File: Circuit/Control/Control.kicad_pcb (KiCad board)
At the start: 2 copper layers, 25.4 x 22.9 mm, 12 parts, among them J1 Signal, J2 12V NO G, SW1 Force on, U1 NE555

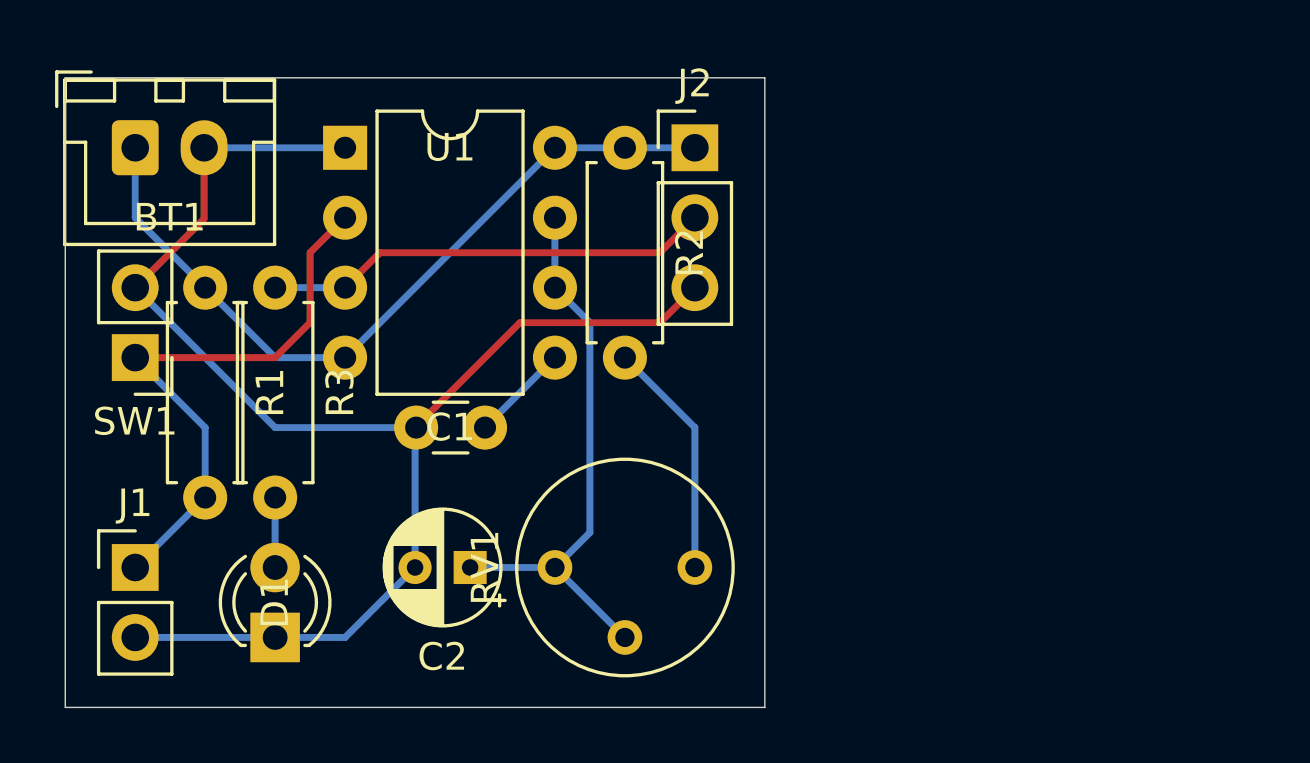
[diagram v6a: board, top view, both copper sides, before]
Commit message: [Circuit] Change the interface between control module, switch module, and discharge signal
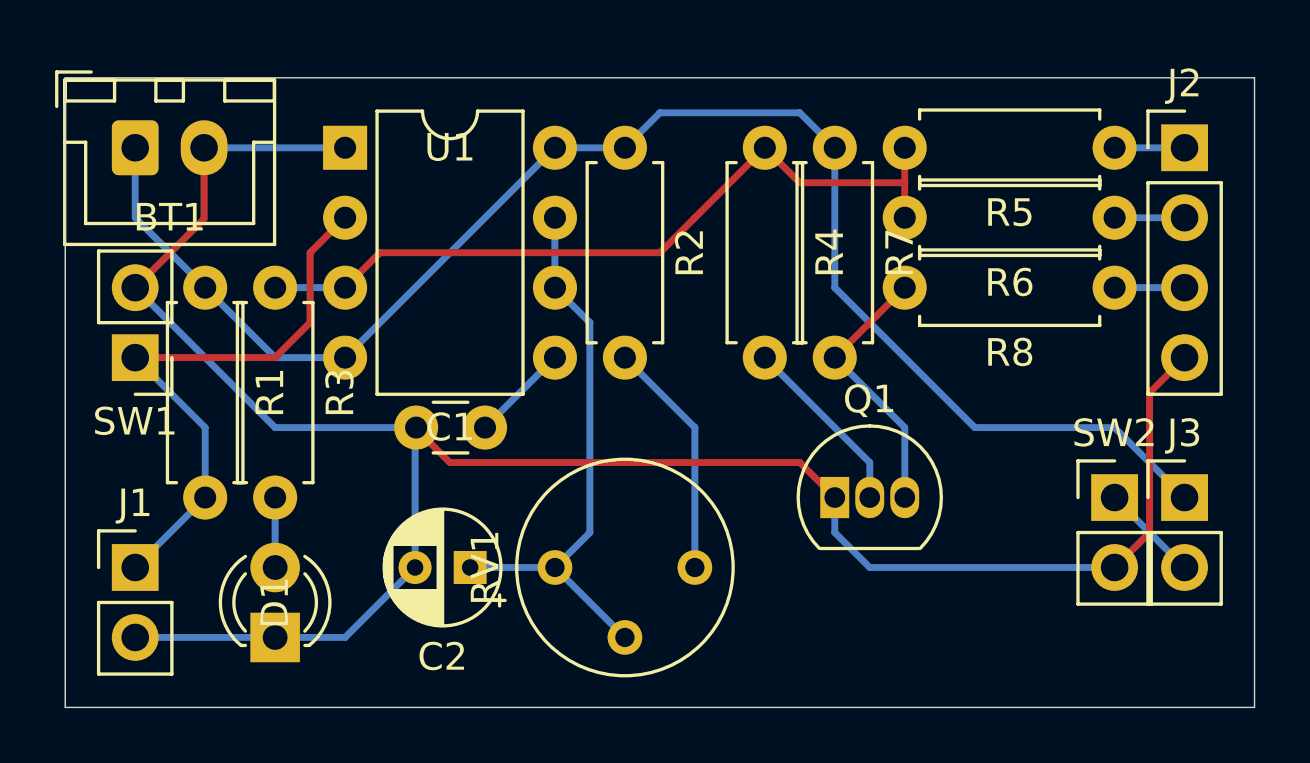
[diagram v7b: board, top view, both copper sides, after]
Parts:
- added J3: Discharge, Connector_PinHeader_2.54mm:PinHeader_1x02_P2.54mm_Vertical, F.Cu at (180.3, 61.0)
- added Q1: 2N3904, Package_TO_SOT_THT:TO-92_Inline, F.Cu at (167.6, 61.0)
- added R4: 3.3K, Resistor_THT:R_Axial_DIN0207_L6.3mm_D2.5mm_P7.62mm_Horizontal, F.Cu at (165.1, 48.3)
- added R5: 1K, Resistor_THT:R_Axial_DIN0207_L6.3mm_D2.5mm_P7.62mm_Horizontal, F.Cu at (177.8, 48.3)
- added R6: 1K, Resistor_THT:R_Axial_DIN0207_L6.3mm_D2.5mm_P7.62mm_Horizontal, F.Cu at (177.8, 50.8)
- added R7: 680, Resistor_THT:R_Axial_DIN0207_L6.3mm_D2.5mm_P7.62mm_Horizontal, F.Cu at (167.6, 48.3)
- added R8: 330, Resistor_THT:R_Axial_DIN0207_L6.3mm_D2.5mm_P7.62mm_Horizontal, F.Cu at (177.8, 53.3)
- added SW2: Discharge, Connector_PinHeader_2.54mm:PinHeader_1x02_P2.54mm_Vertical, F.Cu at (177.8, 61.0)
- J2: value 12V NO G -> To Switch; footprint Connector_PinHeader_2.54mm:PinHeader_1x03_P2.54mm_Vertical -> Connector_PinHeader_2.54mm:PinHeader_1x04_P2.54mm_Vertical
- R3: value 2K -> 2.2K
- moved J2 17.8 mm to (180.3, 48.3)
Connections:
- J1 pad 1: /CapacitorSignal -> /VoltageSensingSignal
- J2 pad 1: +12V -> /CoilSignal
- J2 pad 2: /ControlSignal -> /StarterSignal
- J2 pad 3: GND -> /CapacitorSignal
- R1 pad 2: /CapacitorSignal -> /VoltageSensingSignal
- R3 pad 1: /ControlSignal -> Net-(R3-Pad1)
- SW1 pad 1: /CapacitorSignal -> /VoltageSensingSignal
- U1 pad 2: /CapacitorSignal -> /VoltageSensingSignal
- U1 pad 3: /ControlSignal -> Net-(R3-Pad1)
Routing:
- net Net-(R3-Pad1): track 0.00 -> 28.0 mm
- net +12V: track 28.1 -> 55.2 mm
- net GND: track 52.0 -> 76.7 mm
- net /VoltageSensingSignal: track 0.00 -> 20.9 mm
- net /CapacitorSignal: track 20.9 -> 2.54 mm
- net /ControlSignal: track 16.3 -> 0.00 mm
- net Net-(Q1-Pad3): track 0.00 -> 9.72 mm
- net Net-(Q1-Pad2): track 0.00 -> 6.66 mm
- net /DischargeGND: track 0.00 -> 3.59 mm
- net /StarterSignal: track 0.00 -> 2.54 mm
- net /CoilSignal: track 0.00 -> 2.54 mm
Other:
- board size 25.4 x 22.9 mm -> 43.2 x 22.9 mm

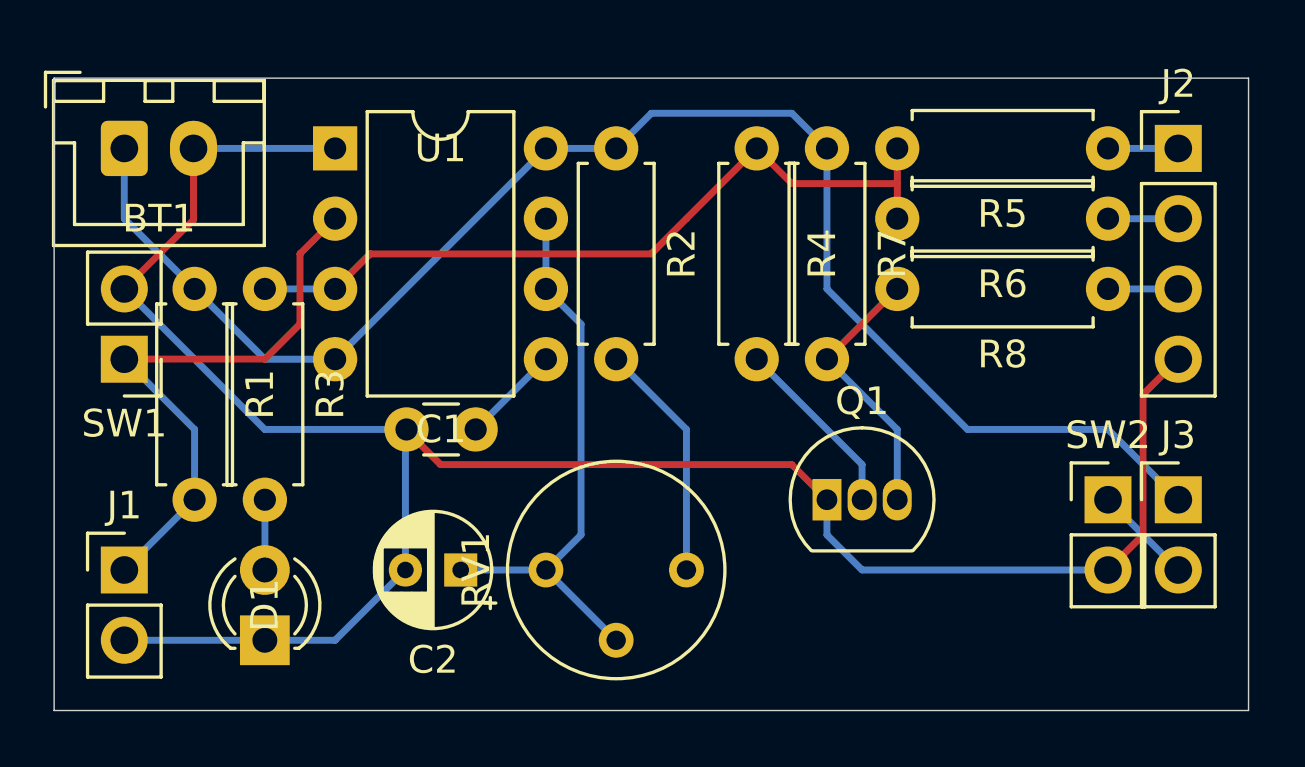
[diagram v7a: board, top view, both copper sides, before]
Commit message: [Circuit] Add propellant injector signal
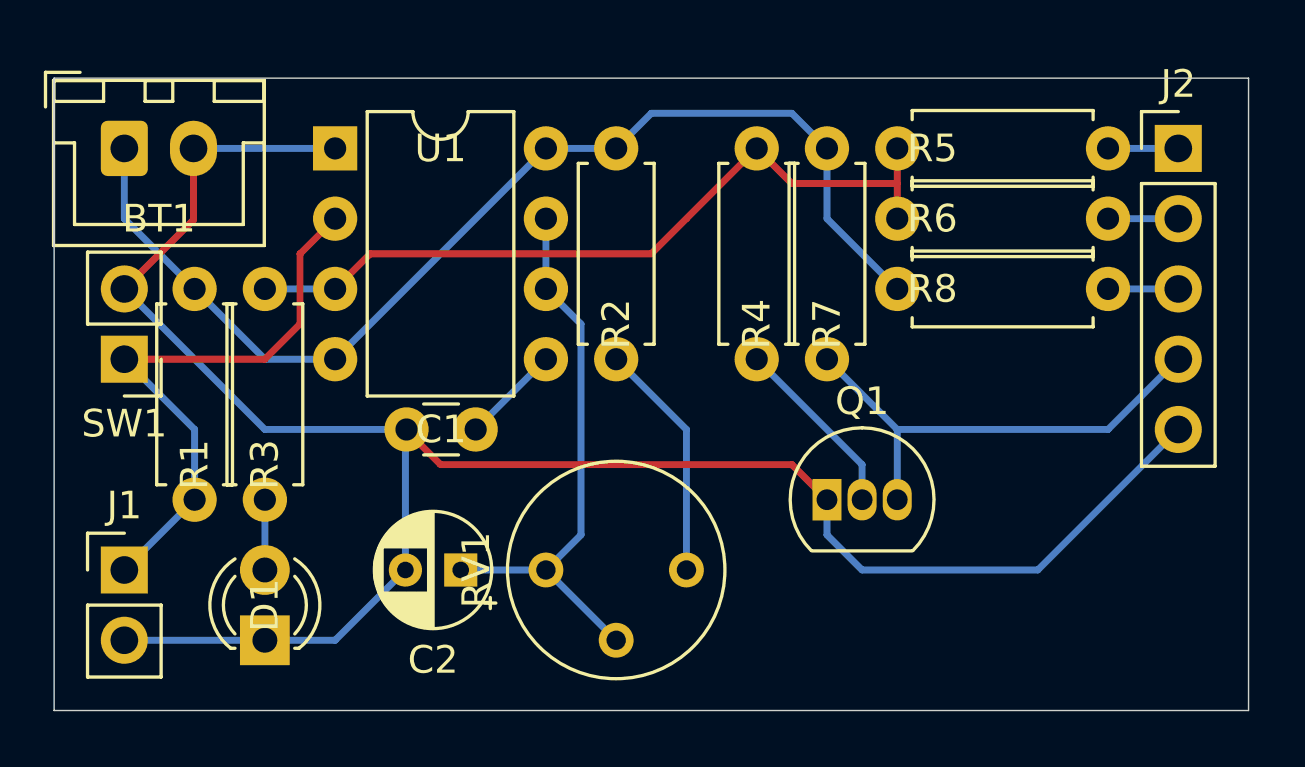
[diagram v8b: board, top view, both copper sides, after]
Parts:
- removed J3, SW2: Discharge, Connector_PinHeader_2.54mm:PinHeader_1x02_P2.54mm_Vertical
- J2: footprint Connector_PinHeader_2.54mm:PinHeader_1x04_P2.54mm_Vertical -> Connector_PinHeader_2.54mm:PinHeader_1x05_P2.54mm_Vertical
- R7: value 680 -> 1K
- R8: value 330 -> 1K
- moved R8 7.62 mm to (170.2, 53.3), turned to 0 degrees
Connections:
- J2 pad 3: /CapacitorSignal -> /PropellantInjectorSignal
- J2 pad 4: GND -> /CapacitorSignal
- Q1 pad 3: Net-(Q1-Pad3) -> /CapacitorSignal
- R7 pad 2: Net-(Q1-Pad3) -> /CapacitorSignal
- R8 pad 1: /CapacitorSignal -> +12V
- R8 pad 2: Net-(Q1-Pad3) -> /PropellantInjectorSignal
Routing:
- net /CapacitorSignal: track 2.54 -> 17.3 mm
- net +12V: track 55.2 -> 40.4 mm
- net Net-(Q1-Pad3): track 9.72 -> 0.00 mm
- net GND: track 76.7 -> 72.7 mm
- net /DischargeGND: track 3.59 -> 0.00 mm
- net /PropellantInjectorSignal: track 0.00 -> 2.54 mm
